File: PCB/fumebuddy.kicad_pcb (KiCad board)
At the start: 2 copper layers, 26.2 x 67.2 mm, 23 parts, among them J1 USB_B_Micro, J2 STATION, J3 FTDI, SW1 SW_SPDT, SW2 SW_SPDT, SW3 FLASH, SW4 SW_OPT, U1 AP7361C-33E, U2 CPC1017N (NO), U4 ESP32-WROOM-32D, U5 CPC1117N (NC)

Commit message: should be v3
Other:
- board text added: "fumebuddy v3"
- board text removed: "fumebuddy v2"
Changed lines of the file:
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@@
     (effects (font (size 1 1) (thickness 0.1)))
   )
-  (gr_text "fumebuddy\nv2" (at 131 144.25) (layer F.SilkS)
+  (gr_text "fumebuddy\nv3" (at 131 144.25) (layer F.SilkS)
     (effects (font (size 1.5 1.5) (thickness 0.2)))
   )

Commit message: Maybe update to new AutoConnect format?
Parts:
- added REF**: TinkerTown_Silkscreen, !Custom:TinkerTown_Silkscreen, F.Cu at (134.4, 111.8)
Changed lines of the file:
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@@
     (tracks 265)
     (zones 0)
-    (modules 23)
+    (modules 24)
     (nets 51)
   )
@@
     (add_net VBUS)
   )
+  (module !Custom:TinkerTown_Silkscreen locked (layer Top)
+    (at 134.4 111.8)
+    (fp_text reference REF** (at 0 4) (layer F.SilkS) hide
+      (effects (font (size 0.5 0.5) (thickness 0.05)))
+    )
+    (fp_text value TinkerTown_Silkscreen (at -0.03 -4.5) (layer F.Fab)
+      (effects (font (size 1 1) (thickness 0.15)))
+    )
+    (fp_line (start 0.81573 -0.82061) (end 0.31179 -0.31653) (layer F.SilkS) (width 0.1))
+    (fp_line (start -2.55481 -0.72607) (end -1.86179 -0.72607) (layer F.SilkS) (width 0.1))
+    (fp_line (start 0.65821 -2.67905) (end 0.65821 -1.8285) (layer F.SilkS) (width 0.1))
+    (fp_line (start -0.49145 -0.09604) (end -0.49145 -0.09604) (layer F.SilkS) (width 0.1))
+    (fp_line (start -1.70373 2.51838) (end -1.70373 3.416172) (layer F.SilkS) (width 0.1))
+    (fp_line (start 1.77747 2.51838) (end 1.77747 3.416172) (layer F.SilkS) (width 0.1))
+    (fp_curve (pts (xy 0.26907 1.44186) (xy 0.26907 1.23005) (xy 0.10686 1.05821) (xy -0.0932 1.05821)) (layer F.SilkS) (width 0.1))
+    (fp_curve (pts (xy -0.45536 1.44186) (xy -0.45536 1.65366) (xy -0.29316 1.82537) (xy -0.0932 1.82537)) (layer F.SilkS) (width 0.1))
+    (fp_curve (pts (xy 1.69782 0.1931) (xy 1.69782 -0.01885) (xy 1.5355 -0.19055) (xy 1.33555 -0.19055)) (layer F.SilkS) (width 0.1))
+    (fp_line (start -2.58 -0.47859) (end -3.515436 -0.47859) (layer F.SilkS) (width 0.1))
+    (fp_line (start -0.46 1.48) (end -1.35771 1.47892) (layer F.SilkS) (width 0.1))
+    (fp_line (start 1.33555 0.5766) (end 1.33555 0.5766) (layer F.SilkS) (width 0.1))
+    (fp_line (start 0.31179 0.43948) (end -2.55481 0.43948) (layer F.SilkS) (width 0.1))
+    (fp_line (start 1.0813 2.51838) (end 1.0813 3.416172) (layer F.SilkS) (width 0.1))
+    (fp_line (start 1.47719 -0.82061) (end 0.81573 -0.82061) (layer F.SilkS) (width 0.1))
+    (fp_curve (pts (xy -0.22013 -0.69823) (xy -0.28656 -0.7732) (xy -0.38357 -0.82061) (xy -0.49145 -0.82061)) (layer F.SilkS) (width 0.1))
+    (fp_line (start -2.58 0.22) (end -3.515436 0.21775) (layer F.SilkS) (width 0.1))
+    (fp_line (start -1.07 -1.38753) (end -1.07 -2.68) (layer F.SilkS) (width 0.1))
+    (fp_line (start -1.86179 -1.38753) (end -1.07 -1.38753) (layer F.SilkS) (width 0.1))
+    (fp_line (start -1.00741 2.51838) (end -1.00741 3.416172) (layer F.SilkS) (width 0.1))
+    (fp_line (start -1.64 1.76) (end -2.58 1.76) (layer F.SilkS) (width 0.1))
+    (fp_line (start -1.35771 1.47892) (end -1.6413 1.76) (layer F.SilkS) (width 0.1))
+    (fp_curve (pts (xy 0.97325 0.1931) (xy 0.97325 0.40487) (xy 1.13545 0.5766) (xy 1.33555 0.5766)) (layer F.SilkS) (width 0.1))
+    (fp_line (start -0.0932 1.82537) (end -0.0932 1.82537) (layer F.SilkS) (width 0.1))
+    (fp_curve (pts (xy -0.0932 1.82537) (xy 0.10686 1.82537) (xy 0.26907 1.65366) (xy 0.26907 1.44186)) (layer F.SilkS) (width 0.1))
+    (fp_line (start 1.47719 -2.68) (end 1.47719 -0.82061) (layer F.SilkS) (width 0.1))
+    (fp_line (start 0.31179 -0.31653) (end 0.31179 0.43948) (layer F.SilkS) (width 0.1))
+    (fp_line (start 0.38495 2.51838) (end 0.38495 3.416172) (layer F.SilkS) (width 0.1))
+    (fp_curve (pts (xy -0.0932 1.05821) (xy -0.29316 1.05821) (xy -0.45536 1.23005) (xy -0.45536 1.44186)) (layer F.SilkS) (width 0.1))
+    (fp_line (start 0.65821 -1.8285) (end -0.24 -0.71) (layer F.SilkS) (width 0.1))
+    (fp_line (start 1.35523 1.21944) (end 1.67 1.54) (layer F.SilkS) (width 0.1))
+    (fp_line (start 1.67 1.54) (end 1.67 2.49) (layer F.SilkS) (width 0.1))
+    (fp_curve (pts (xy 1.33555 -0.19055) (xy 1.13545 -0.19055) (xy 0.97325 -0.01885) (xy 0.97325 0.1931)) (layer F.SilkS) (width 0.1))
+    (fp_line (start 1.35523 0.589551) (end 1.35523 1.21944) (layer F.SilkS) (width 0.1))
+    (fp_curve (pts (xy -0.853761 -0.45831) (xy -0.853761 -0.25821) (xy -0.69155 -0.09604) (xy -0.49145 -0.09604)) (layer F.SilkS) (width 0.1))
+    (fp_curve (pts (xy -0.12933 -0.45831) (xy -0.12933 -0.55038) (xy -0.163651 -0.63445) (xy -0.22013 -0.69823)) (layer F.SilkS) (width 0.1))
+    (fp_line (start -1.86179 -0.72607) (end -1.86179 -1.38753) (layer F.SilkS) (width 0.1))
+    (fp_curve (pts (xy 1.33555 0.5766) (xy 1.5355 0.5766) (xy 1.69782 0.40487) (xy 1.69782 0.1931)) (layer F.SilkS) (width 0.1))
+    (fp_line (start -0.31122 2.51838) (end -0.31122 3.416172) (layer F.SilkS) (width 0.1))
+    (fp_curve (pts (xy -0.49145 -0.09604) (xy -0.29153 -0.09604) (xy -0.12933 -0.25821) (xy -0.12933 -0.45831)) (layer F.SilkS) (width 0.1))
+    (fp_curve (pts (xy -0.49145 -0.82061) (xy -0.69155 -0.82061) (xy -0.853761 -0.6584) (xy -0.853761 -0.45831)) (layer F.SilkS) (width 0.1))
+    (fp_line (start -1.00741 -3.56939) (end -1.00741 -2.68) (layer F.SilkS) (width 0.1))
+    (fp_line (start -2.58 0.913931) (end -3.515436 0.913931) (layer F.SilkS) (width 0.1))
+    (fp_line (start -2.58 1.61025) (end -3.515436 1.61025) (layer F.SilkS) (width 0.1))
+    (fp_line (start 3.52468 -0.47859) (end 2.62703 -0.47859) (layer F.SilkS) (width 0.1))
+    (fp_line (start 3.52468 -1.17477) (end 2.62703 -1.17477) (layer F.SilkS) (width 0.1))
+    (fp_line (start 3.52468 1.61025) (end 2.62703 1.61025) (layer F.SilkS) (width 0.1))
+    (fp_curve (pts (xy -2.57754 1.73) (xy -2.57754 1.73) (xy -2.57754 2.51756) (xy -1.79 2.51756)) (layer F.SilkS) (width 0.1))
+    (fp_line (start -2.58 -1.17477) (end -3.515436 -1.17477) (layer F.SilkS) (width 0.1))
+    (fp_line (start 0.38495 -3.56939) (end 0.38495 -2.68) (layer F.SilkS) (width 0.1))
+    (fp_line (start -2.58 -1.87094) (end -3.515436 -1.87094) (layer F.SilkS) (width 0.1))
+    (fp_line (start 3.52468 0.21775) (end 2.62703 0.21775) (layer F.SilkS) (width 0.1))
+    (fp_line (start 1.77747 -3.56939) (end 1.77747 -2.69) (layer F.SilkS) (width 0.1))
+    (fp_line (start 3.52468 0.913931) (end 2.62703 0.913931) (layer F.SilkS) (width 0.1))
+    (fp_line (start 3.52468 -1.87094) (end 2.62703 -1.87094) (layer F.SilkS) (width 0.1))
+    (fp_line (start -0.31122 -3.56939) (end -0.31122 -2.68) (layer F.SilkS) (width 0.1))
+    (fp_line (start 1.08 -3.56) (end 1.08 -2.69) (layer F.SilkS) (width 0.1))
+    (fp_line (start -1.70373 -3.56939) (end -1.71 -2.69) (layer F.SilkS) (width 0.1))
+    (fp_line (start 1.83247 -2.68) (end -1.79 -2.68) (layer F.SilkS) (width 0.1))
+    (fp_line (start 2.62001 1.73) (end 2.62001 -1.89246) (layer F.SilkS) (width 0.1))
+    (fp_curve (pts (xy 1.83247 2.51756) (xy 1.83247 2.51756) (xy 2.62001 2.51756) (xy 2.62001 1.73)) (layer F.SilkS) (width 0.1))
+    (fp_curve (pts (xy 2.62001 -1.89246) (xy 2.62001 -1.89246) (xy 2.62001 -2.68) (xy 1.83247 -2.68)) (layer F.SilkS) (width 0.1))
+    (fp_line (start -1.79 2.51756) (end 1.83247 2.51756) (layer F.SilkS) (width 0.1))
+    (fp_line (start -2.57754 -1.89246) (end -2.57754 1.73) (layer F.SilkS) (width 0.1))
+    (fp_curve (pts (xy -1.79 -2.68) (xy -1.79 -2.68) (xy -2.57754 -2.68) (xy -2.57754 -1.89246)) (layer F.SilkS) (width 0.1))
+  )
   (module !Custom:FTDI-3Pin (layer Bottom)

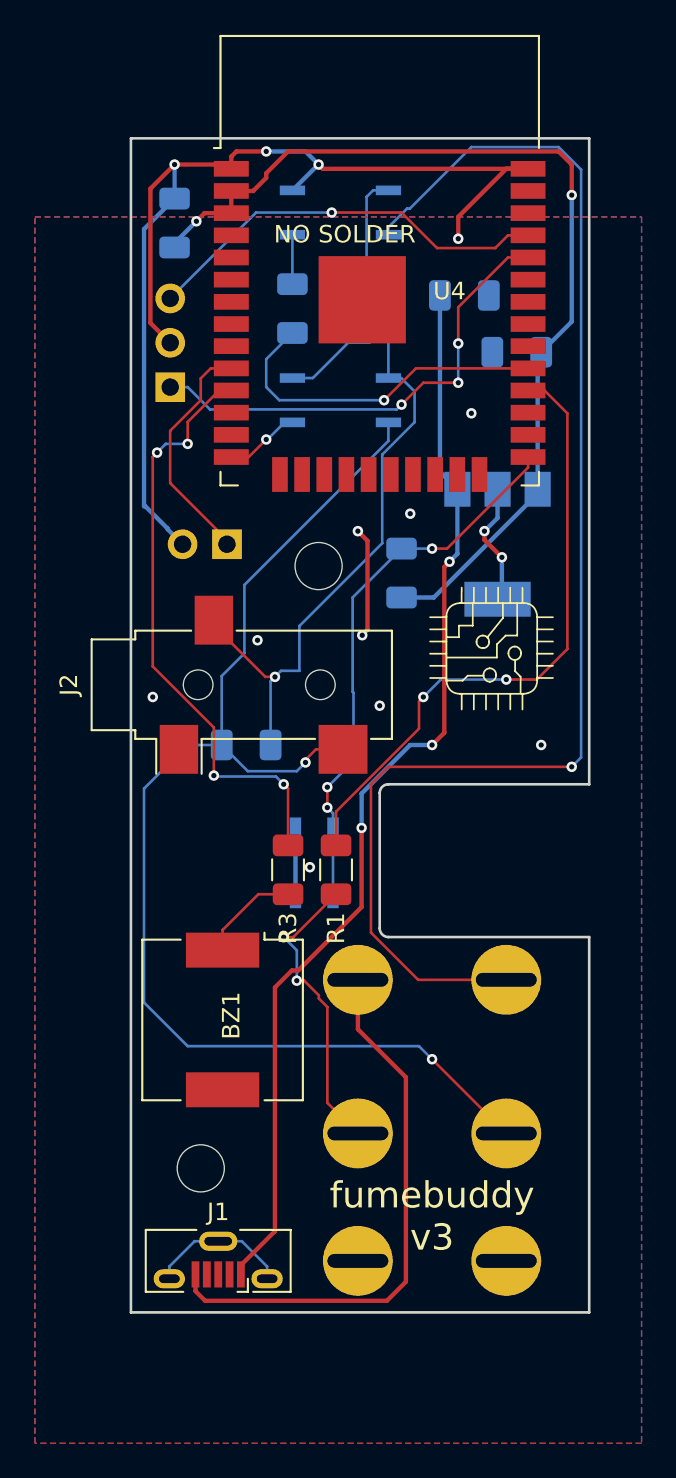
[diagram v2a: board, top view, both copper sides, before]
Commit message: Move to one-sided for all SMD components
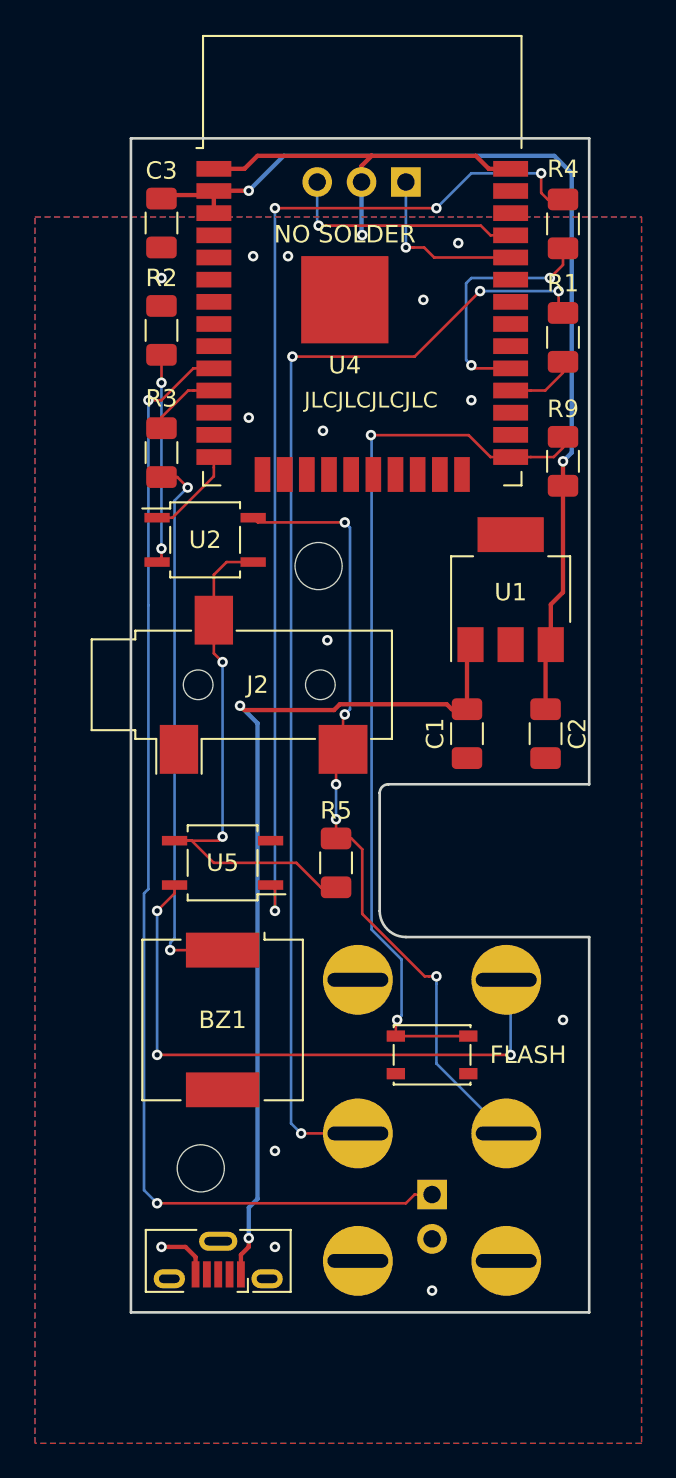
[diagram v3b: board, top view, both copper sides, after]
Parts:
- C1, C2, C3, R2, R4, R5, R9, U1, U2, U5: moved to F.Cu
- FLASH: renamed from SW3; moved to F.Cu
- REF**: moved to B.Cu
- moved SW4 39.1 mm to (131.0, 143.0), turned to 180 degrees
- moved U5 37.9 mm to (119.0, 124.0), turned to 180 degrees
- moved R1 33.2 mm to (138.5, 93.9), turned to 90 degrees
- moved C1 25.1 mm to (133.0, 116.6), turned to 90 degrees
- moved R3 25.0 mm to (115.5, 100.5)
- moved C2 21.9 mm to (137.5, 116.6), turned to 270 degrees
- moved J3 17.9 mm to (129.5, 85.0), turned to 90 degrees
- moved R4 16.2 mm to (138.5, 87.4)
- moved FLASH 12.9 mm to (131.0, 135.0), turned to 0 degrees
- moved R2 11.3 mm to (115.5, 93.5)
- moved R9 11.2 mm to (138.5, 101.0)
- moved U2 11.1 mm to (118.0, 105.5)
- moved R5 8.49 mm to (125.5, 124.0), turned to 90 degrees
- moved U1 2.71 mm to (135.5, 108.3), turned to 90 degrees
- moved REF** 1.58 mm to (133.5, 110.5)
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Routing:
- net GND: track 114.5 -> 25.6 mm
- net Net-(R4-Pad2): track 2.83 -> 60.4 mm, vias 0 -> 4
- net Net-(SW4-Pad1): track 13.6 -> 66.9 mm, vias 0 -> 2
- net Net-(R1-Pad2): track 17.3 -> 66.2 mm, vias 2 -> 4
- net Net-(SW1-Pad1): track 77.6 -> 34.8 mm, vias 1 -> 3
- net /SENSOR: track 36.3 -> 4.05 mm, vias 2 -> 0
- net Net-(R3-Pad2): track 34.3 -> 4.34 mm, vias 4 -> 0
- net Net-(J2-PadT): track 72.2 -> 46.0 mm, vias 2 -> 5
- net Net-(BZ1-Pad1): track 5.75 -> 31.7 mm, vias 0 -> 2
- net Net-(R9-Pad1): track 31.8 -> 51.8 mm, vias 3 -> 2
- net /RXD: track 27.2 -> 9.99 mm, vias 3 -> 1
- net Net-(J2-PadR): track 43.4 -> 31.0 mm, vias 1 -> 2
- net VBUS: track 62.6 -> 50.5 mm, vias 3 -> 2
- net /TXD: track 23.7 -> 13.8 mm
- net Net-(J1-Pad6): track 8.20 -> 0.00 mm
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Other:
- outline, holes or cut-outs redrawn
- board text added: "JLCJLCJLCJLC"
- board text added: "fumebuddy v4"
- board text removed: "fumebuddy v3"
